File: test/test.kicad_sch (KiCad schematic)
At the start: 5 parts, among them J1 Conn_01x10_Male, J2 Conn_01x04_Male, J3 Conn_01x04_Male, U1 74HC157, U2 74HC00

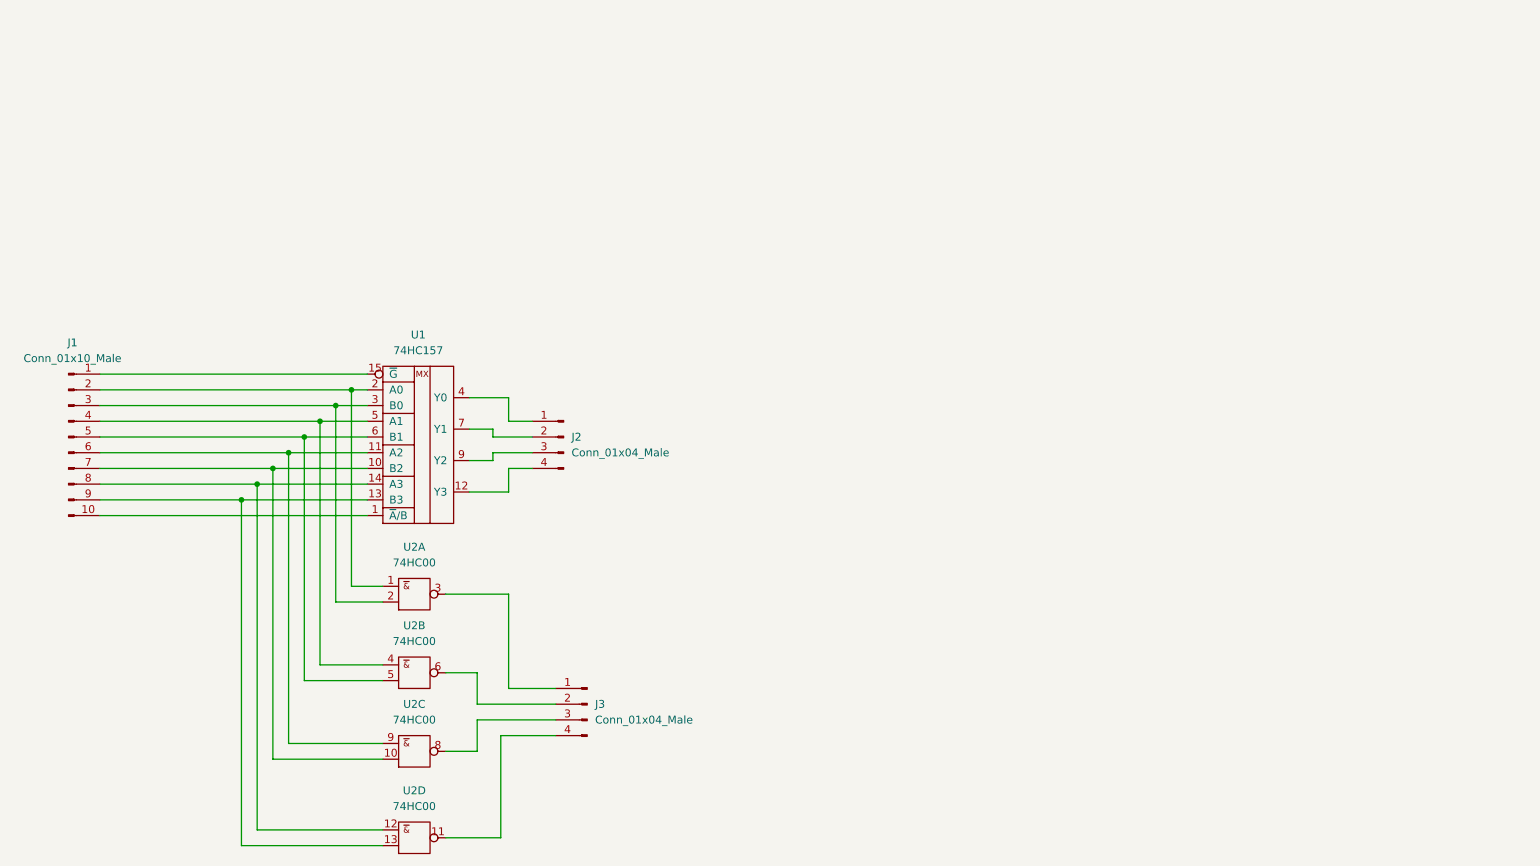
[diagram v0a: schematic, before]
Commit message: add keyboard
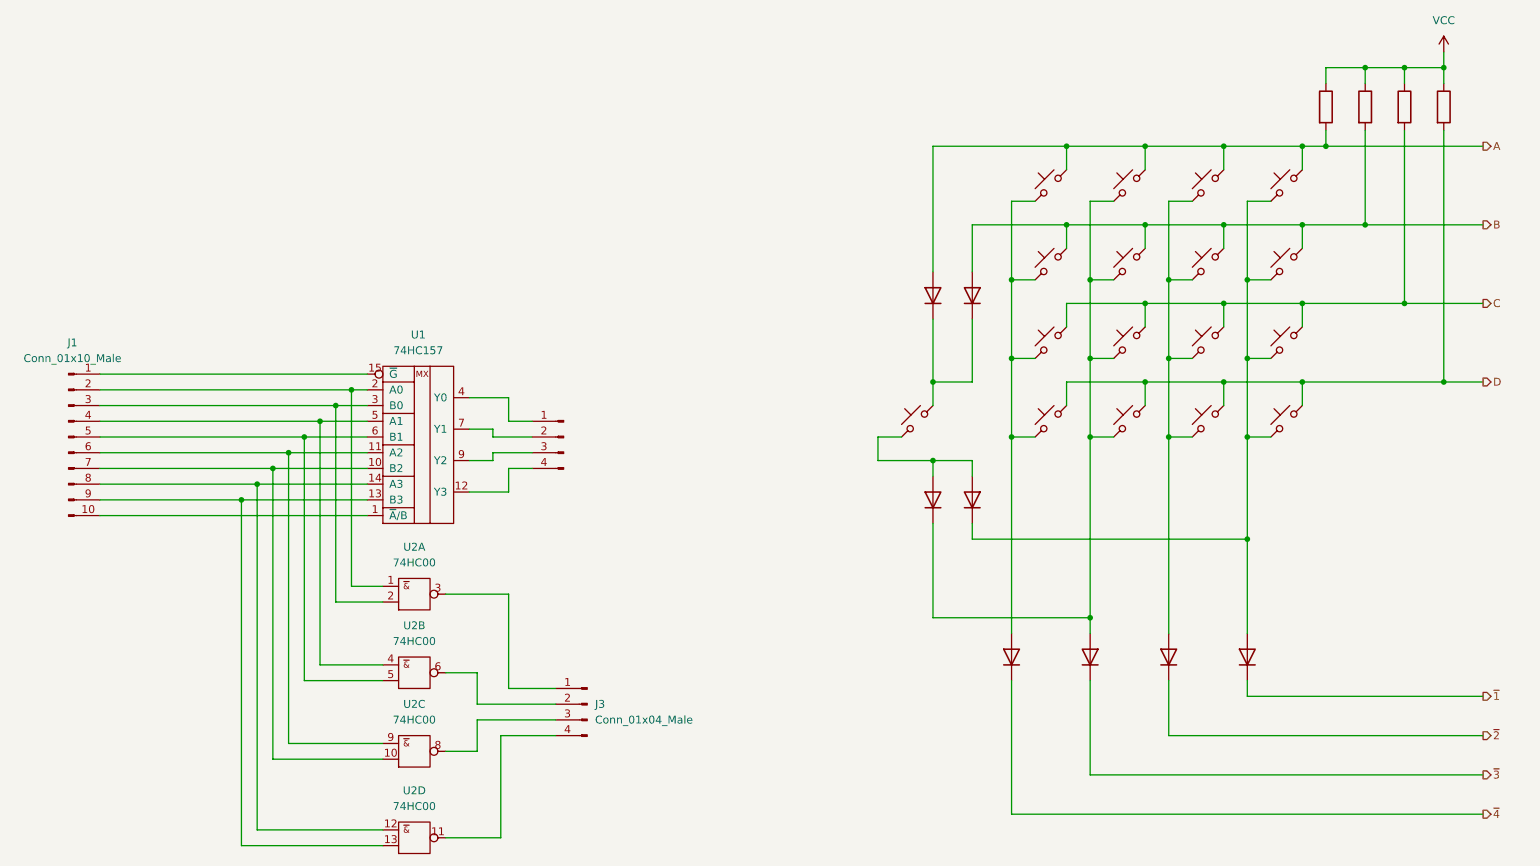
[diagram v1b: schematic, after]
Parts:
- added D? (x8): DIODE, symbol Simulation_SPICE:DIODE
- added R? (x4): R, symbol Device:R
- added SW? (x17): SW_Push_45deg, symbol Switch:SW_Push_45deg
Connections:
- net VCC: now also R?.1, R?.1, R?.1, R?.1
- new net: D?.1 (A), SW?.2, SW?.2, SW?.2, SW?.2 (x2)
- new net: D?.2 (K), D?.2 (K), SW?.1
- new net: D?.1 (A), D?.1 (A), SW?.2
- new net: D?.1 (A), D?.2 (K), SW?.2, SW?.2, SW?.2, SW?.2 (x2)
- new net A: D?.1 (A), R?.2, SW?.1, SW?.1, SW?.1, SW?.1
- new net B: D?.1 (A), R?.2, SW?.1, SW?.1, SW?.1, SW?.1
- new net C: R?.2, SW?.1, SW?.1, SW?.1, SW?.1
- new net D: R?.2, SW?.1, SW?.1, SW?.1, SW?.1
- new net ~{1}: D?.2 (K)
- new net ~{2}: D?.2 (K)
- new net ~{3}: D?.2 (K)
- new net ~{4}: D?.2 (K)

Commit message: update stlink update ZX-keyboard updeate test
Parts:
- removed D? (x8): DIODE, symbol Simulation_SPICE:DIODE
- removed J1: Conn_01x10_Male, Connector_PinHeader_2.54mm:PinHeader_1x10_P2.54mm_Vertical, symbol Connector:Conn_01x10_Male
- removed J2, J3: Conn_01x04_Male, Connector_PinHeader_2.54mm:PinHeader_1x04_P2.54mm_Vertical, symbol Connector:Conn_01x04_Male
- removed R? (x4): R, symbol Device:R
- removed SW? (x17): SW_Push_45deg, symbol Switch:SW_Push_45deg
- removed U1: 74HC157, Package_DIP:DIP-16_W7.62mm, symbol 74IEC:74HC157
- removed U2: 74HC00, symbol 74IEC:74HC00
- added D?: LED, symbol Device:LED
- added R?: 470, symbol Device:R
- added RV? (x2): 22k, symbol Device:R_Potentiometer
- added U?: LM311, symbol Comparator:LM311
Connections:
- net GND: now also RV?.3, RV?.3, U?.1 (GND), U?.4 (V-)
- net VCC: now also R?.1, RV?.1, RV?.1, U?.8 (V+)
- new net: RV?.2, U?.2 (+)
- new net: RV?.2, U?.3 (-)
- new net: D?.1 (K), U?.7
- new net: D?.2 (A), R?.2
